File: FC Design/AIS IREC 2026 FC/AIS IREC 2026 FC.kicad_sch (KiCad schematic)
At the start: 66 parts, among them IC1 ADXL314WBCPZ-RL, IC2 MT29F8G08ABACAWP-IT_C_TR, J1 USB4216-03-A, J2 EBAA-02-C, J3 Conn_01x08, J4 EBAA-02-C, J5 EBAA-02-C, Q1 MMBT3906-TP, Q2 DMN2008LFU-7, Q3 DMN2008LFU-7, U1 STM32F205VBTx, U2 KC2520Z, U3 AZ1117-1.8, U4 AZ1117-3.3, U5 MS5607-02BA, U6 USB3300-EZK

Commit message: Fucking hell
All of the routing. All of the fucking routing.
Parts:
- removed C24, C25: 100nF, SamacSys_Parts:GRM022C81C222KE01L, symbol SamacSys_Parts:GRM022R61A104KE01L
- removed LED2, LED3: 598-8D91-127F, SamacSys_Parts:5988D91127F, symbol SamacSys_Parts:598-8D91-127F
- removed R4, R6: 10KR, Resistor_SMD:R_0201_0603Metric, symbol Device:R
- added C23: 100nF, SamacSys_Parts:GRM022C81C222KE01L, symbol SamacSys_Parts:GRM022R61A104KE01L
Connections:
- net 3.3V: now also Q2.1 (S1), Q2.4 (S2), Q3.1 (S1), Q3.4 (S2), C23.1
- net GND: now also C23.2
- net Vsrc: no longer Q2.1 (S1), Q2.4 (S2), Q3.1 (S1), Q3.4 (S2)

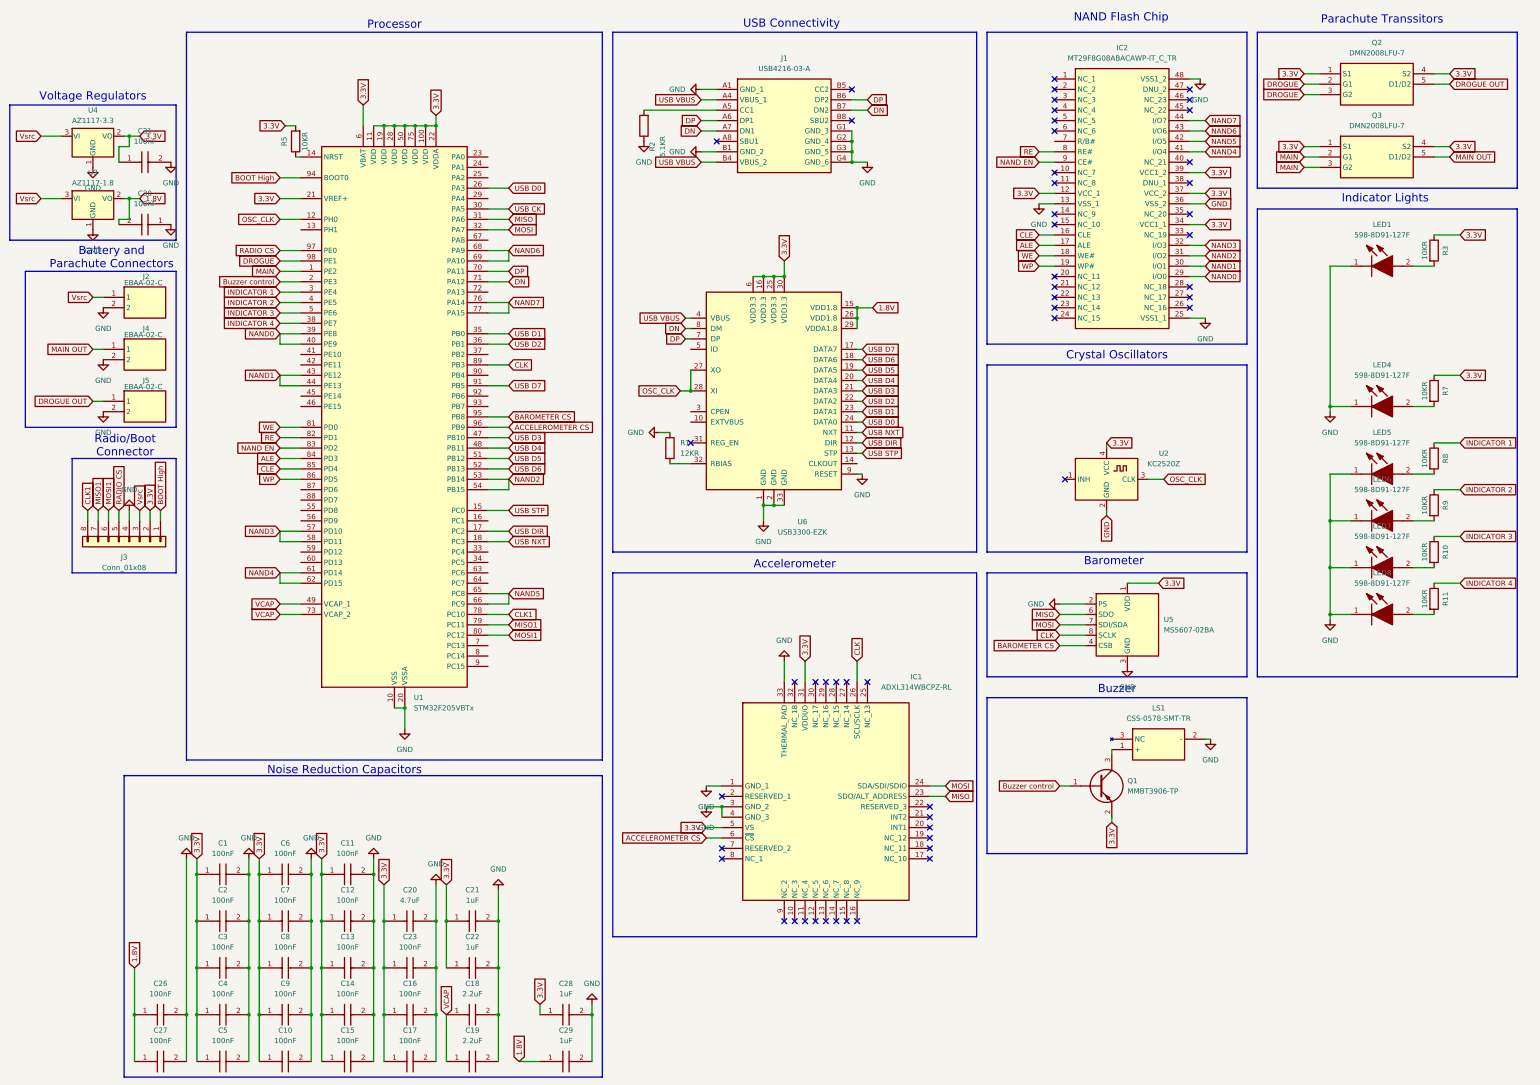
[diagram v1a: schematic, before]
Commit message: Changed from usb fs and hs to just usb fs, made appropriate changes
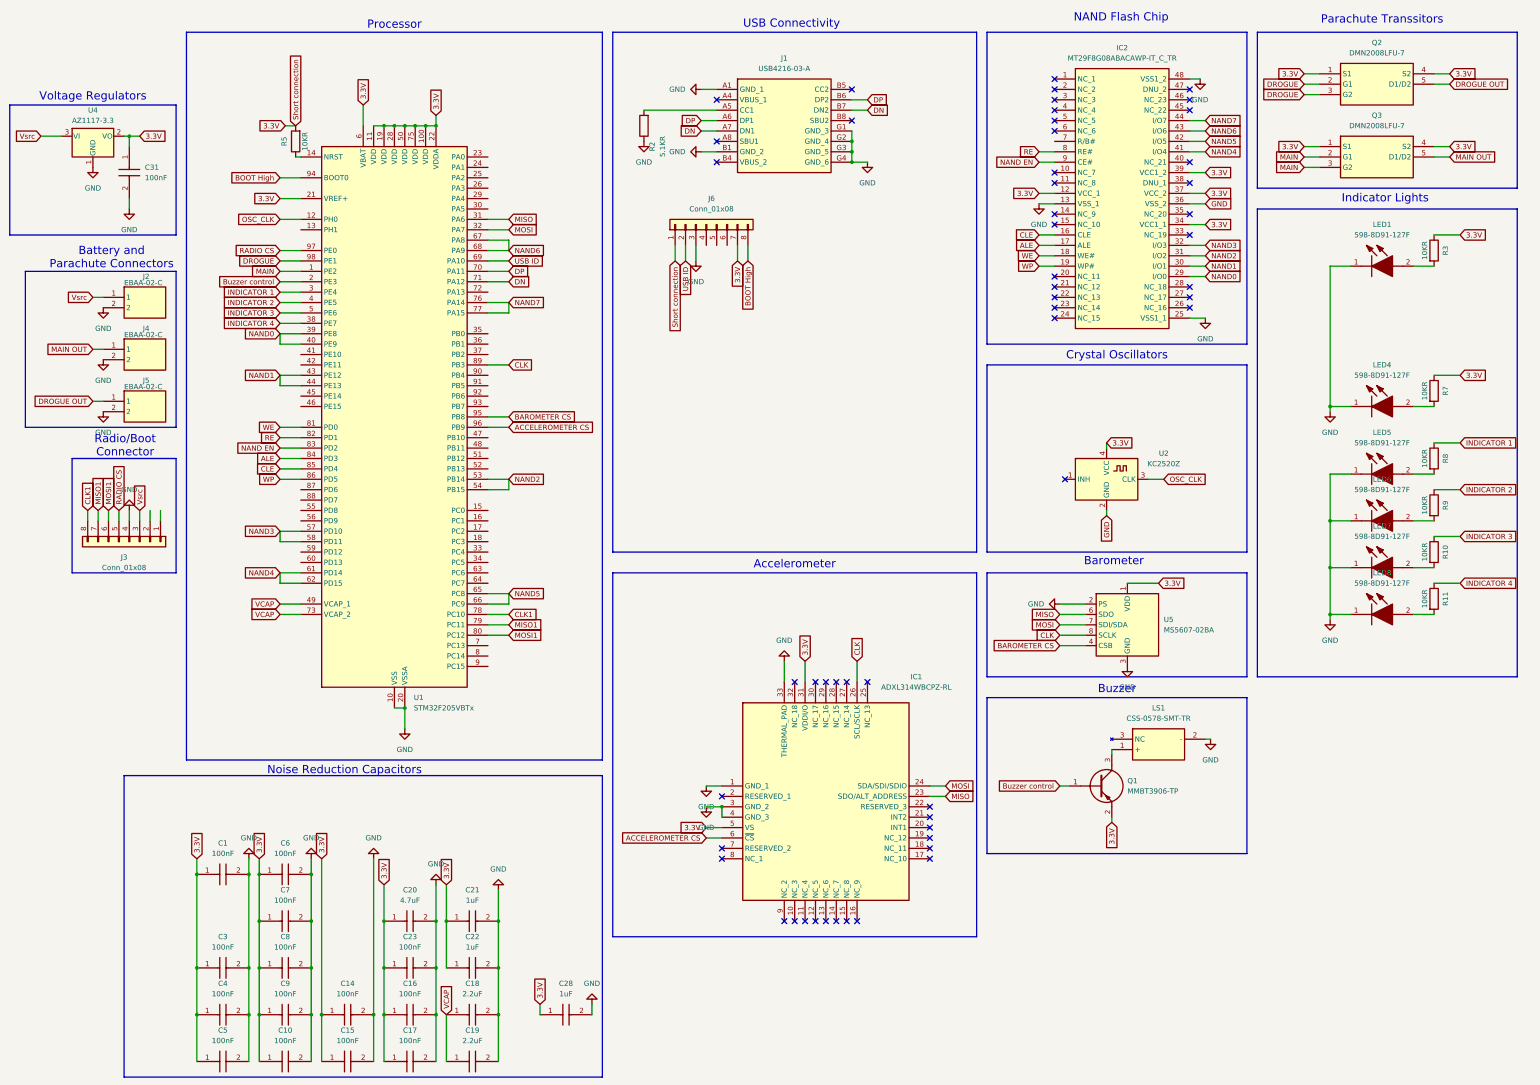
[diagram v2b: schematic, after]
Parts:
- removed C11, C12, C13, C2, C26, C27, C30: 100nF, SamacSys_Parts:GRM022C81C222KE01L, symbol SamacSys_Parts:GRM022R61A104KE01L
- removed C29: 1uF, SamacSys_Parts:CAPC0603X33N, symbol SamacSys_Parts:GRT033R60J105ME13D
- removed R1: 12KR, Resistor_SMD:R_0201_0603Metric, symbol Device:R
- removed U3: AZ1117-1.8, Package_TO_SOT_SMD:SOT-223-3_TabPin2, symbol Regulator_Linear:AZ1117-1.8
- removed U6: USB3300-EZK, Package_DFN_QFN:QFN-32-1EP_5x5mm_P0.5mm_EP3.45x3.45mm, symbol Interface_USB:USB3300-EZK
- added J6: Conn_01x08, Connector_Hirose:Hirose_DF13-08P-1.25DSA_1x08_P1.25mm_Vertical, symbol Connector_Generic:Conn_01x08
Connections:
- net 3.3V: now also J6.1 (Pin_1), J6.7 (Pin_7); no longer J3.2 (Pin_2)
- net BOOT High: now also J6.8 (Pin_8); no longer J3.1 (Pin_1)
- net GND: now also J6.3 (Pin_3)
- net NAND6: now also U1.67 (PA8); no longer U1.69 (PA10)
- net USB CK: no longer names the net of U1.30 (PA5)
- net USB D0: no longer names the net of U1.26 (PA3)
- net USB D1: no longer names the net of U1.35 (PB0)
- net USB D2: no longer names the net of U1.36 (PB1)
- net USB D3: no longer names the net of U1.47 (PB10)
- net USB D4: no longer names the net of U1.48 (PB11)
- net USB D5: no longer names the net of U1.51 (PB12)
- net USB D6: no longer names the net of U1.52 (PB13)
- net USB D7: no longer names the net of U1.91 (PB5)
- net USB DIR: no longer names the net of U1.17 (PC2)
- net USB NXT: no longer names the net of U1.18 (PC3)
- net USB STP: no longer names the net of U1.15 (PC0)
- net USB VBUS: no longer names the net of J1.A4 (VBUS_1)
- net USB VBUS: no longer J1.B4 (VBUS_2)
- new net USB ID: J6.2 (Pin_2), U1.69 (PA10)
- no-connect marks 53 -> 54
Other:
- moved on the sheet: C31

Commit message: Got PCB to a state where I'm happy for Logan to look at it before manufacture
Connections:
- net 3.3V: now also J3.3 (Pin_3)
- net Vsrc: no longer J3.3 (Pin_3)
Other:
- moved on the sheet: C1
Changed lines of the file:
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@@
 	)
 	(junction
-		(at 78.74 231.14)
+		(at 78.74 242.57)
 		(diameter 0)
 		(color 0 0 0 0)
@@
 	)
 	(junction
-		(at 66.04 231.14)
+		(at 66.04 242.57)
 		(diameter 0)
 		(color 0 0 0 0)
@@
 	(wire
 		(pts
-			(xy 66.04 231.14) (xy 66.04 254)
+			(xy 66.04 242.57) (xy 66.04 254)
 		)
 		(stroke
@@
 	(wire
 		(pts
-			(xy 109.22 227.33) (xy 109.22 265.43)
+			(xy 109.22 261.62) (xy 109.22 265.43)
 		)
 		(stroke
@@
 	(wire
 		(pts
-			(xy 78.74 231.14) (xy 78.74 254)
+			(xy 78.74 242.57) (xy 78.74 254)
 		)
 		(stroke
@@
 	(wire
 		(pts
-			(xy 66.04 227.33) (xy 66.04 231.14)
+			(xy 66.04 238.76) (xy 66.04 242.57)
 		)
 		(stroke
@@
 	(wire
 		(pts
-			(xy 78.74 227.33) (xy 78.74 231.14)
+			(xy 78.74 238.76) (xy 78.74 242.57)
 		)
 		(stroke
@@
 	(wire
 		(pts
-			(xy 96.52 227.33) (xy 96.52 265.43)
+			(xy 96.52 261.62) (xy 96.52 265.43)
 		)
 		(stroke
@@
 	(global_label "3.3V"
 		(shape input)
-		(at 66.04 227.33 90)
+		(at 66.04 238.76 90)
 		(fields_autoplaced yes)
 		(effects
@@
 		)
 		(property "Intersheetrefs" "${INTERSHEET_REFS}"
-			(at 66.04 220.2324 90)
+			(at 66.04 231.6624 90)
 			(effects
 				(font
@@
 		)
 	)
-	(global_label "Vsrc"
+	(global_label "3.3V"
 		(shape input)
 		(at 52.07 142.24 90)
@@
 		)
 		(property "Intersheetrefs" "${INTERSHEET_REFS}"
-			(at 52.07 135.2633 90)
+			(at 52.07 135.1424 90)
 			(effects
 				(font
@@
 	(global_label "3.3V"
 		(shape input)
-		(at 96.52 227.33 90)
+		(at 96.52 261.62 90)
 		(fields_autoplaced yes)
 		(effects
@@
 		)
 		(property "Intersheetrefs" "${INTERSHEET_REFS}"
-			(at 96.52 220.2324 90)
+			(at 96.52 254.5224 90)
 			(effects
 				(font
@@
 	(symbol
 		(lib_id "SamacSys_Parts:GRM022R61A104KE01L")
-		(at 66.04 231.14 0)
+		(at 66.04 242.57 0)
 		(unit 1)
 		(exclude_from_sim no)
@@
 		(fields_autoplaced yes)
 		(property "Reference" "C1"
-			(at 72.39 223.52 0)
+			(at 72.39 234.95 0)
 			(effects
 				(font
@@
 		)
 		(property "Value" "100nF"
-			(at 72.39 226.06 0)
+			(at 72.39 237.49 0)
 			(effects
 				(font
@@
 		)
 		(property "Footprint" "SamacSys_Parts:GRM022C81C222KE01L"
-			(at 74.93 327.33 0)
+			(at 74.93 338.76 0)
 			(effects
 				(font
@@
 		)
 		(property "Datasheet" "https://search.murata.co.jp/Ceramy/image/img/A01X/G101/ENG/GRM022R61A104KE01-01A.pdf"
-			(at 74.93 427.33 0)
+			(at 74.93 438.76 0)
 			(effects
 				(font
@@
 		)
 		(property "Description" "Capacitor Ceramic Multilayer (MLCC)"
-			(at 66.04 231.14 0)
+			(at 66.04 242.57 0)
 			(effects
 				(font
@@
 		)
 		(property "Height" "0.22"
-			(at 74.93 627.33 0)
+			(at 74.93 638.76 0)
 			(effects
 				(font
@@
 		)
 		(property "Mouser Part Number" "81-GRM022R61A104KE1L"
-			(at 74.93 727.33 0)
+			(at 74.93 738.76 0)
 			(effects
 				(font
@@
 		)
 		(property "Mouser Price/Stock" "https://www.mouser.co.uk/ProductDetail/Murata-Electronics/GRM022R61A104KE01L?qs=d0WKAl%252BL4KbGNEA7c9Dbcw%3D%3D"
-			(at 74.93 827.33 0)
+			(at 74.93 838.76 0)
 			(effects
 				(font
@@
 		)
 		(property "Manufacturer_Name" "Murata Electronics"
-			(at 74.93 927.33 0)
+			(at 74.93 938.76 0)
 			(effects
 				(font
@@
 		)
 		(property "Manufacturer_Part_Number" "GRM022R61A104KE01L"
-			(at 74.93 1027.33 0)
+			(at 74.93 1038.76 0)
 			(effects
 				(font
@@
 	(symbol
 		(lib_id "power:GND")
-		(at 78.74 227.33 180)
+		(at 78.74 238.76 180)
 		(unit 1)
 		(exclude_from_sim no)
@@
 		(fields_autoplaced yes)
 		(property "Reference" "#PWR06"
-			(at 78.74 220.98 0)
+			(at 78.74 232.41 0)
 			(effects
 				(font
@@
 		)
 		(property "Value" "GND"
-			(at 78.74 222.25 0)
+			(at 78.74 233.68 0)
 			(effects
 				(font
@@
 		)
 		(property "Footprint" ""
-			(at 78.74 227.33 0)
+			(at 78.74 238.76 0)
 			(effects
 				(font
@@
 		)
 		(property "Datasheet" ""
-			(at 78.74 227.33 0)
+			(at 78.74 238.76 0)
 			(effects
 				(font
@@
 		)
 		(property "Description" "Power symbol creates a global label with name \"GND\" , ground"
-			(at 78.74 227.33 0)
+			(at 78.74 238.76 0)
 			(effects
 				(font
@@
 	(symbol
 		(lib_id "power:GND")
-		(at 109.22 227.33 180)
+		(at 109.22 261.62 180)
 		(unit 1)
 		(exclude_from_sim no)
@@
 		(fields_autoplaced yes)
 		(property "Reference" "#PWR08"
-			(at 109.22 220.98 0)
+			(at 109.22 255.27 0)
 			(effects
 				(font
@@
 		)
 		(property "Value" "GND"
-			(at 109.22 222.25 0)
+			(at 109.22 256.54 0)
 			(effects
 				(font
@@
 		)
 		(property "Footprint" ""
-			(at 109.22 227.33 0)
+			(at 109.22 261.62 0)
 			(effects
 				(font
@@
 		)
 		(property "Datasheet" ""
-			(at 109.22 227.33 0)
+			(at 109.22 261.62 0)
 			(effects
 				(font
@@
 		)
 		(property "Description" "Power symbol creates a global label with name \"GND\" , ground"
-			(at 109.22 227.33 0)
+			(at 109.22 261.62 0)
 			(effects
 				(font
